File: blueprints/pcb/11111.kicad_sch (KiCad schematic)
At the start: 63 parts, among them SW1 SW_Push, SW10 SW_Push, SW11 SW_Push, SW12 SW_Push, SW13 SW_Push, SW14 SW_Push, SW15 SW_Push, SW16 SW_Push, SW17 SW_Push, SW18 SW_Push, SW19 SW_Push, SW2 SW_Push, SW20 SW_Push, SW21 SW_Push, SW22 SW_Push, SW23 SW_Push, SW24 SW_Push, SW25 SW_Push, SW26 SW_Push, SW27 SW_Push, SW28 SW_Push, SW29 SW_Push, SW3 SW_Push, SW30 SW_Push, SW31 SW_Push, SW4 SW_Push, SW5 SW_Push, SW6 SW_Push, SW7 SW_Push, SW8 SW_Push, SW9 SW_Push

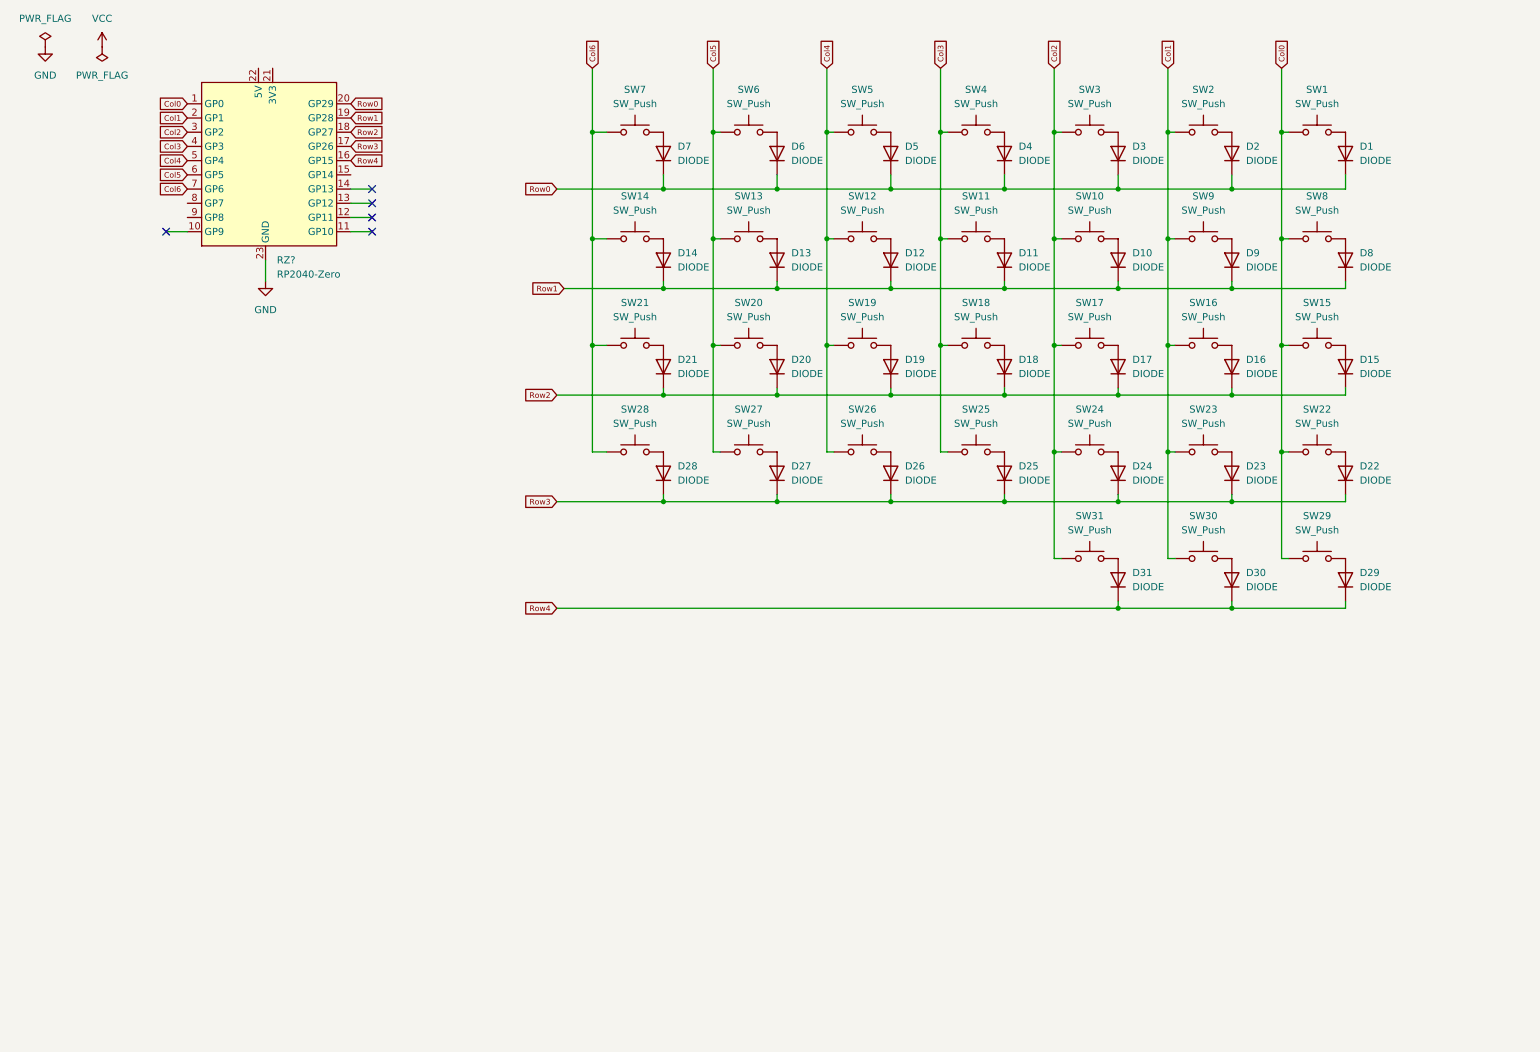
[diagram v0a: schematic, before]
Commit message: update schematic
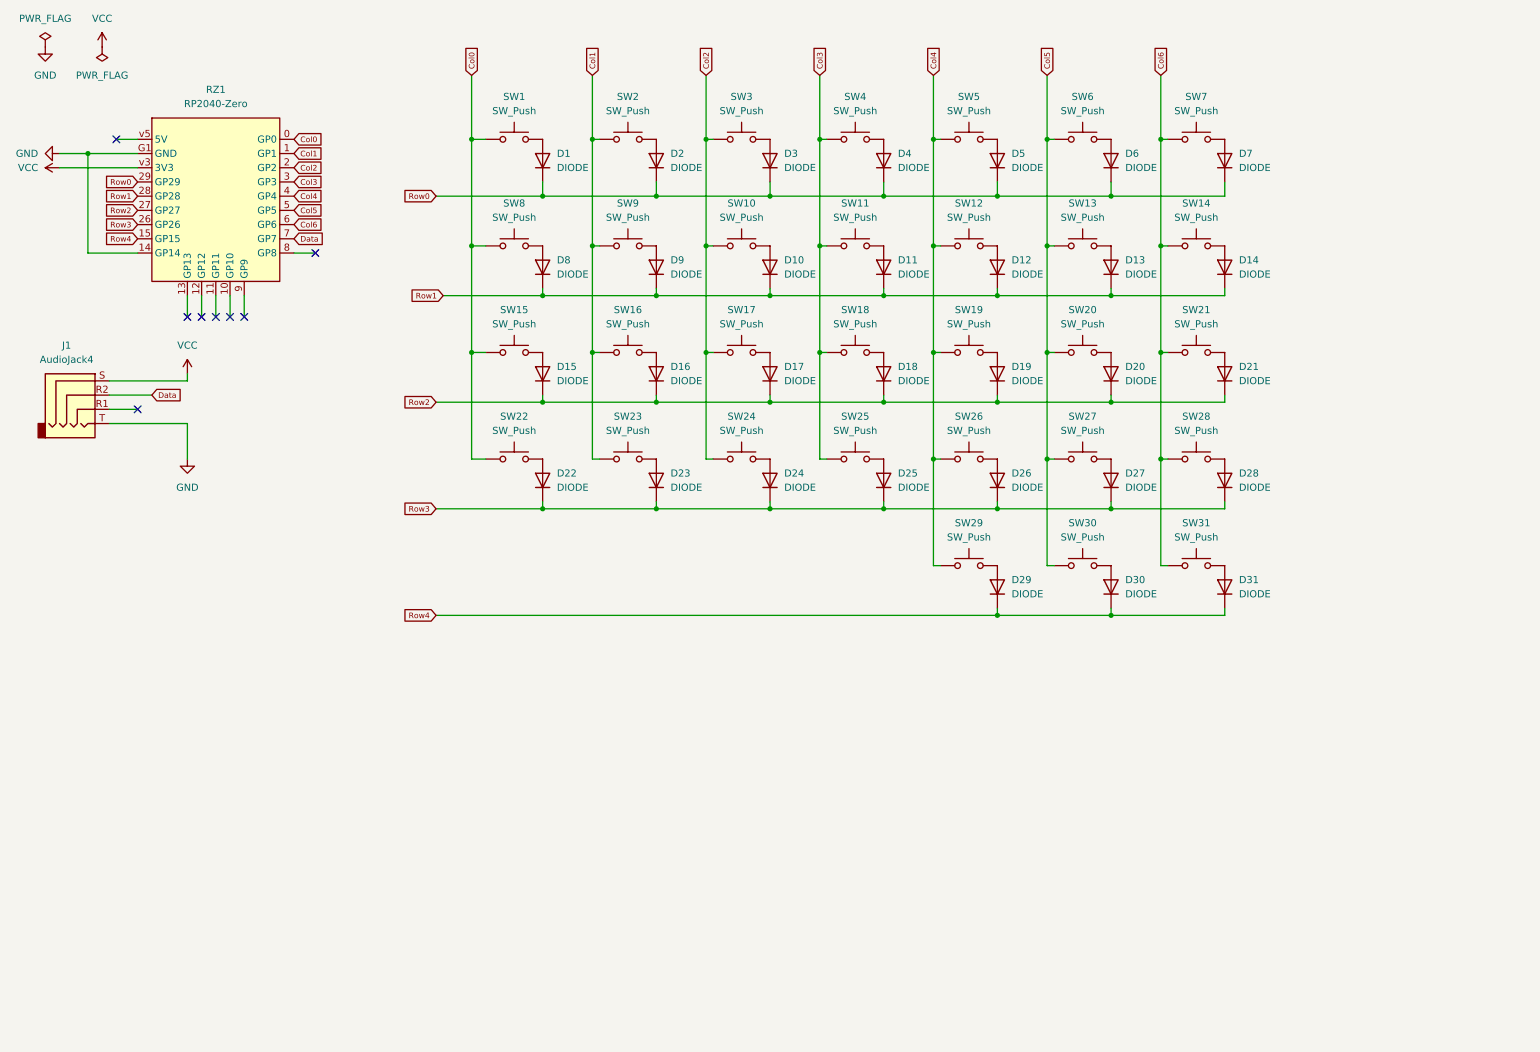
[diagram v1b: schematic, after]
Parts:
- removed RZ?: RP2040-Zero, symbol RP2040-zero:RP2040-Zero
- added J1: AudioJack4, symbol Connector:AudioJack4
- added RZ1: RP2040-Zero, symbol keyboard_utils:RP2040-Zero
- renumbered D7 to D1, D12 to D10, D10 to D12, D9 to D13, D8 to D14, D21 to D15, D20 to D16, D19 to D17, D17 to D19, D6 to D2, D16 to D20, D15 to D21, D28 to D22, D27 to D23, D26 to D24, D24 to D26, D23 to D27, D22 to D28, D31 to D29, D5 to D3, D29 to D31, D3 to D5, D2 to D6, D1 to D7, D14 to D8, D13 to D9, SW7 to SW1, SW12 to SW10, SW10 to SW12, SW9 to SW13, SW8 to SW14, SW21 to SW15, SW20 to SW16, SW19 to SW17, SW17 to SW19, SW6 to SW2, SW16 to SW20, SW15 to SW21, SW28 to SW22, SW27 to SW23, SW26 to SW24, SW24 to SW26, SW23 to SW27, SW22 to SW28, SW31 to SW29, SW5 to SW3, SW29 to SW31, SW3 to SW5, SW2 to SW6, SW1 to SW7, SW14 to SW8, SW13 to SW9
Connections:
- net Col0: now also SW1.1, SW15.1, SW22.1, SW8.1, RZ1.0 (GP0); no longer SW14.1, SW21.1, SW28.1, SW31.1, SW7.1
- net Col1: now also SW16.1, SW2.1, SW23.1, SW9.1, RZ1.1 (GP1); no longer SW13.1, SW20.1, SW27.1, SW30.1, SW6.1
- net Col2: now also SW10.1, SW17.1, SW24.1, SW3.1, RZ1.2 (GP2); no longer SW12.1, SW19.1, SW26.1, SW29.1, SW5.1
- net Col3: now also RZ1.3 (GP3)
- net Col4: now also SW12.1, SW19.1, SW26.1, SW29.1, SW5.1, RZ1.4 (GP4); no longer SW10.1, SW17.1, SW24.1, SW3.1
- net Col5: now also SW13.1, SW20.1, SW27.1, SW30.1, SW6.1, RZ1.5 (GP5); no longer SW16.1, SW2.1, SW23.1, SW9.1
- net Col6: now also SW14.1, SW21.1, SW28.1, SW31.1, SW7.1, RZ1.6 (GP6); no longer SW1.1, SW15.1, SW22.1, SW8.1
- net GND: now also J1.T, RZ1.14 (GP14), RZ1.G1 (GND)
- net Row0: now also RZ1.29 (GP29)
- net Row1: now also RZ1.28 (GP28)
- net Row2: now also RZ1.27 (GP27)
- net Row3: now also RZ1.26 (GP26)
- net Row4: now also RZ1.15 (GP15)
- net VCC: now also J1.S, RZ1.v3 (3V3)
- new net Data: J1.R2, RZ1.7 (GP7)
- no-connect marks 5 -> 8
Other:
- moved on the sheet: D1, D10, D11, D12, D13, D14, D15, D16, D17, D18, D19, D2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

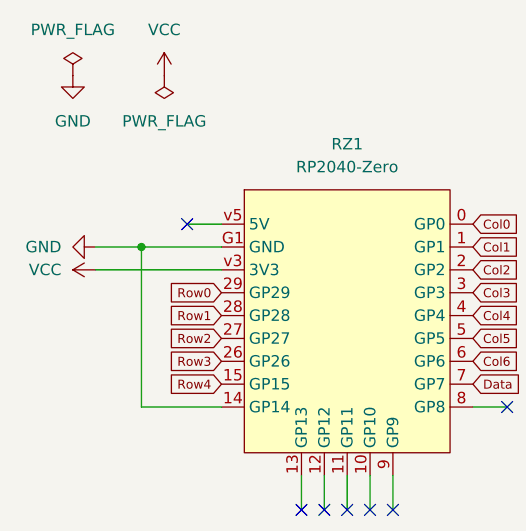
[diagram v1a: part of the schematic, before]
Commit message: fix VCC pin
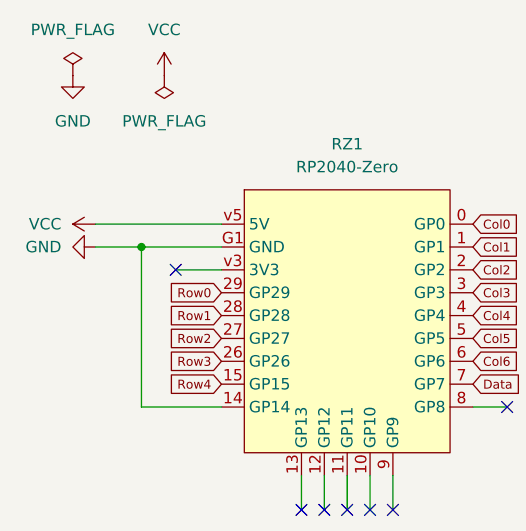
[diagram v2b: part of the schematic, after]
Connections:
- net VCC: now also RZ1.v5 (5V); no longer RZ1.v3 (3V3)
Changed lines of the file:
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@@
   (junction (at 156.21 35.56) (diameter 0) (color 0 0 0 0)
   )
+  (no_connect (at 29.21 40.64))
   (no_connect (at 34.29 83.82))
-  (no_connect (at 30.48 35.56))
   (no_connect (at 45.72 67.31))
   (no_connect (at 66.04 55.88))
@@
     (stroke (width 0) (type default) (color 0 0 0 0))
   )
+  (wire (pts (xy 29.21 40.64) (xy 34.29 40.64))
+    (stroke (width 0) (type default) (color 0 0 0 0))
+  )
   (wire (pts (xy 135.89 54.61) (xy 137.16 54.61))
     (stroke (width 0) (type default) (color 0 0 0 0))
@@
     (stroke (width 0) (type default) (color 0 0 0 0))
   )
-  (wire (pts (xy 20.32 40.64) (xy 34.29 40.64))
-    (stroke (width 0) (type default) (color 0 0 0 0))
-  )
   (wire (pts (xy 228.6 100.33) (xy 228.6 101.6))
     (stroke (width 0) (type default) (color 0 0 0 0))
@@
     (stroke (width 0) (type default) (color 0 0 0 0))
   )
-  (wire (pts (xy 30.48 35.56) (xy 34.29 35.56))
+  (wire (pts (xy 20.32 35.56) (xy 34.29 35.56))
     (stroke (width 0) (type default) (color 0 0 0 0))
   )
@@
     (pin "2")
   )
+  (symbol (lib_id "power:VCC") (at 20.32 35.56 90) (unit 1)
+    (in_bom yes) (on_board yes) (fields_autoplaced)
+    (property "Reference" "#PWR0101" (id 0) (at 24.13 35.56 0)
+      (effects (font (size 1.27 1.27)) hide)
+    )
+    (property "Value" "VCC" (id 1) (at 16.51 35.5599 90)
+      (effects (font (size 1.27 1.27)) (justify left))
+    )
+    (property "Footprint" "" (id 2) (at 20.32 35.56 0)
+      (effects (font (size 1.27 1.27)) hide)
+    )
+    (property "Datasheet" "" (id 3) (at 20.32 35.56 0)
+      (effects (font (size 1.27 1.27)) hide)
+    )
+    (pin "1")
+  )
   (symbol (lib_id "Simulation_SPICE:DIODE") (at 228.6 96.52 270) (unit 1)
     (in_bom yes) (on_board yes) (fields_autoplaced)
@@
     (pin "1")
     (pin "2")
-  )
-  (symbol (lib_id "power:VCC") (at 20.32 40.64 90) (unit 1)
-    (in_bom yes) (on_board yes) (fields_autoplaced)
-    (property "Reference" "#PWR04" (id 0) (at 24.13 40.64 0)
-      (effects (font (size 1.27 1.27)) hide)
-    )
-    (property "Value" "VCC" (id 1) (at 16.51 40.6399 90)
-      (effects (font (size 1.27 1.27)) (justify left))
-    )
-    (property "Footprint" "" (id 2) (at 20.32 40.64 0)
-      (effects (font (size 1.27 1.27)) hide)
-    )
-    (property "Datasheet" "" (id 3) (at 20.32 40.64 0)
-      (effects (font (size 1.27 1.27)) hide)
-    )
-    (pin "1")
   )
   (symbol (lib_id "Switch:SW_Push") (at 101.6 54.61 0) (unit 1)
@@
       (reference "#PWR03") (unit 1) (value "GND") (footprint "")
     )
-    (path "/3b3ce66b-f504-499c-85a4-01d45057655b"
-      (reference "#PWR04") (unit 1) (value "VCC") (footprint "")
-    )
     (path "/5d431e12-648e-4940-bc8a-c8c5f2abe31f"
       (reference "#PWR05") (unit 1) (value "VCC") (footprint "")
@@
       (reference "#PWR06") (unit 1) (value "GND") (footprint "")
     )
+    (path "/16000328-56eb-4afc-9c2f-38337521e33f"
+      (reference "#PWR0101") (unit 1) (value "VCC") (footprint "")
+    )
     (path "/3924bbc6-f984-40eb-8e95-2329eaba9f5e"

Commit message: add right schematic
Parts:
- removed D1, D10, D11, D12, D13, D14, D15, D16, D17, D18, D19, D2, D20, D21, D22, D23, D24, D25, D26, D27, D28, D29, D3, D30, D31, D4, D5, D6, D7, D8, D9: DIODE, symbol Simulation_SPICE:DIODE
- added D1, D10, D11, D12, D13, D14, D15, D16, D17, D18, D19, D2, D20, D21, D22, D23, D24, D25, D26, D27, D28, D29, D3, D30, D31, D32, D33, D34, D35, D36, D37, D38, D39, D4, D40, D41, D42, D43, D44, D45, D46, D47, D48, D49, D5, D50, D51, D52, D53, D54, D55, D56, D57, D58, D59, D6, D60, D61, D62, D7, D8, D9: 1N4148W, Diode_SMD:D_SOD-123, symbol Diode:1N4148W
- added J2: AudioJack4, symbol Connector:AudioJack4
- added RZ2: RP2040-Zero, symbol keyboard_utils:RP2040-Zero
- added SW10, SW11, SW12, SW13, SW14, SW22, SW23, SW24, SW25, SW26, SW27, SW28, SW36, SW37, SW38, SW39, SW40, SW41, SW42, SW50, SW51, SW52, SW53, SW54, SW55, SW56, SW60, SW61, SW62, SW8, SW9: SW_Push, symbol Switch:SW_Push
- renumbered SW8 to SW15, SW9 to SW16, SW10 to SW17, SW11 to SW18, SW12 to SW19, SW13 to SW20, SW14 to SW21, SW15 to SW29, SW16 to SW30, SW17 to SW31, SW18 to SW32, SW19 to SW33, SW20 to SW34, SW21 to SW35, SW22 to SW43, SW23 to SW44, SW24 to SW45, SW25 to SW46, SW26 to SW47, SW27 to SW48, SW28 to SW49, SW29 to SW57, SW30 to SW58, SW31 to SW59
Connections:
- net Row0: now also D1.1 (K), D2.1 (K), D3.1 (K), D4.1 (K), D5.1 (K), D6.1 (K), D7.1 (K)
- net Row1: now also D15.1 (K), D16.1 (K), D17.1 (K), D18.1 (K), D19.1 (K), D20.1 (K), D21.1 (K)
- net Row2: now also D29.1 (K), D30.1 (K), D31.1 (K), D32.1 (K), D33.1 (K), D34.1 (K), D35.1 (K)
- net Row3: now also D43.1 (K), D44.1 (K), D45.1 (K), D46.1 (K), D47.1 (K), D48.1 (K), D49.1 (K)
- net Row4: now also D57.1 (K), D58.1 (K), D59.1 (K)
- net at SW32.2: now also D32.2 (A)
- net at SW16.2: now also D16.2 (A)
- net at SW57.2: now also D57.2 (A)
- net at SW3.2: now also D3.2 (A)
- net at SW7.2: now also D7.2 (A)
- net at SW31.2: now also D31.2 (A)
- net at SW20.2: now also D20.2 (A)
- net at SW29.2: now also D29.2 (A)
- net at SW49.2: now also D49.2 (A)
- net at SW6.2: now also D6.2 (A)
- net at SW34.2: now also D34.2 (A)
- net at SW45.2: now also D45.2 (A)
- net at SW1.2: now also D1.2 (A)
- net at SW33.2: now also D33.2 (A)
- net at SW15.2: now also D15.2 (A)
- net at SW43.2: now also D43.2 (A)
- net at SW35.2: now also D35.2 (A)
- net at SW47.2: now also D47.2 (A)
- net at SW59.2: now also D59.2 (A)
- net at SW21.2: now also D21.2 (A)
- net at SW17.2: now also D17.2 (A)
- net at SW46.2: now also D46.2 (A)
- net at SW18.2: now also D18.2 (A)
- net at SW44.2: now also D44.2 (A)
- net at SW48.2: now also D48.2 (A)
- net at SW5.2: now also D5.2 (A)
- net at SW4.2: now also D4.2 (A)
- net at SW2.2: now also D2.2 (A)
- net at SW58.2: now also D58.2 (A)
- net at SW30.2: now also D30.2 (A)
- net at SW19.2: now also D19.2 (A)
- net Data renamed DataLeft
- new net: D13.2 (A), SW13.2
- new net: D25.2 (A), SW25.2
- new net: D56.2 (A), SW56.2
- new net: D40.2 (A), SW40.2
- new net: D23.2 (A), SW23.2
- new net: D14.2 (A), SW14.2
- new net: D28.2 (A), SW28.2
- new net: D55.2 (A), SW55.2
- new net: D37.2 (A), SW37.2
- new net: D50.2 (A), SW50.2
- new net: D42.2 (A), SW42.2
- new net: D52.2 (A), SW52.2
- new net: D22.2 (A), SW22.2
- new net: D54.2 (A), SW54.2
- new net: D26.2 (A), SW26.2
- new net: D8.2 (A), SW8.2
- new net: D62.2 (A), SW62.2
- new net: D41.2 (A), SW41.2
- new net: D61.2 (A), SW61.2
- new net: D38.2 (A), SW38.2
- new net: D10.2 (A), SW10.2
- new net: D39.2 (A), SW39.2
- new net: D24.2 (A), SW24.2
- new net: D9.2 (A), SW9.2
- new net: D60.2 (A), SW60.2
- new net: D27.2 (A), SW27.2
- new net: D11.2 (A), SW11.2
- new net: D51.2 (A), SW51.2
- new net: D12.2 (A), SW12.2
- new net: D53.2 (A), SW53.2
- new net: D36.2 (A), SW36.2
- new net Col10: RZ2.3 (GP3), SW11.1, SW25.1, SW39.1, SW53.1
- new net Col11: RZ2.4 (GP4), SW12.1, SW26.1, SW40.1, SW54.1, SW60.1
- new net Col12: RZ2.5 (GP5), SW13.1, SW27.1, SW41.1, SW55.1, SW61.1
- new net Col13: RZ2.6 (GP6), SW14.1, SW28.1, SW42.1, SW56.1, SW62.1
- new net Col7: RZ2.0 (GP0), SW22.1, SW36.1, SW50.1, SW8.1
- new net Col8: RZ2.1 (GP1), SW23.1, SW37.1, SW51.1, SW9.1
- new net Col9: RZ2.2 (GP2), SW10.1, SW24.1, SW38.1, SW52.1
- new net DataRight: J2.R2, RZ2.7 (GP7)
- new net GNDA: J2.T, RZ2.G1 (GND)
- new net Row5: D10.1 (K), D11.1 (K), D12.1 (K), D13.1 (K), D14.1 (K), D8.1 (K), D9.1 (K), RZ2.29 (GP29)
- new net Row6: D22.1 (K), D23.1 (K), D24.1 (K), D25.1 (K), D26.1 (K), D27.1 (K), D28.1 (K), RZ2.28 (GP28)
- new net Row7: D36.1 (K), D37.1 (K), D38.1 (K), D39.1 (K), D40.1 (K), D41.1 (K), D42.1 (K), RZ2.27 (GP27)
- new net Row8: D50.1 (K), D51.1 (K), D52.1 (K), D53.1 (K), D54.1 (K), D55.1 (K), D56.1 (K), RZ2.26 (GP26)
- new net Row9: D60.1 (K), D61.1 (K), D62.1 (K), RZ2.15 (GP15)
- new net VDD: J2.S, RZ2.14 (GP14), RZ2.v5 (5V)
- no-connect marks 8 -> 16
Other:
- moved on the sheet: J1, RZ1, SW1, SW15, SW16, SW17, SW18, SW19, SW2, SW20, SW21, SW29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

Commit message: update schematic
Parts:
- J1, J2: value AudioJack4 -> MJ-4PP-9; footprint (none) -> foostan:MJ-4PP-9
- RZ1, RZ2: footprint (none) -> RP2040-zero:rp2040-zero
- SW1, SW10, SW11, SW12, SW13, SW14, SW15, SW16, SW17, SW18, SW19, SW2, SW20, SW21, SW22, SW23, SW24, SW25, SW26, SW27, SW28, SW29, SW3, SW30, SW31, SW32, SW33, SW34, SW35, SW36, SW37, SW38, SW39, SW4, SW40, SW41, SW42, SW43, SW44, SW45, SW46, SW47, SW48, SW49, SW5, SW50, SW51, SW52, SW53, SW54, SW55, SW56, SW57, SW58, SW59, SW6, SW60, SW61, SW62, SW7, SW8, SW9: footprint (none) -> Button_Switch_Keyboard:SW_Cherry_MX_1.00u_PCB

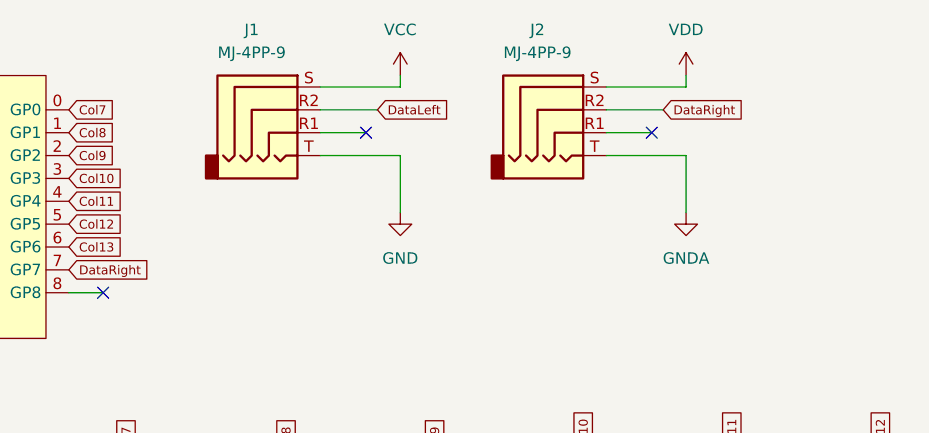
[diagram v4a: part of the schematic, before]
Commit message: use imported symbol for MJ-4PP-9
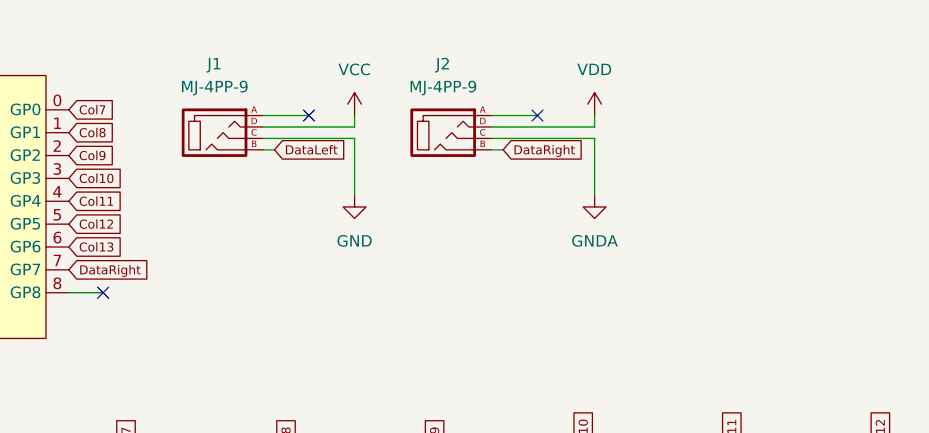
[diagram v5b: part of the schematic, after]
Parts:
- removed J1, J2: MJ-4PP-9, foostan:MJ-4PP-9, symbol Connector:AudioJack4
- added J1, J2: MJ-4PP-9, foostan:MJ-4PP-9_1side, symbol foostan_kbd:MJ-4PP-9
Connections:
- net DataLeft: now also J1.B
- net DataRight: now also J2.B
- net GND: now also J1.C
- net GNDA: now also J2.C
- net VCC: now also J1.D
- net VDD: now also J2.D

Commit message: fix schematic
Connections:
- net Col11: no longer SW60.1
- net Col12: no longer SW61.1
- net Col13: no longer SW62.1
- net Col7: now also SW60.1
- net Col8: now also SW61.1
- net Col9: now also SW62.1
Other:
- moved on the sheet: D60, D61, D62, SW60, SW61, SW62
